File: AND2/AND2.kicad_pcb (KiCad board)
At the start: 2 copper layers, 31.7 x 27.9 mm, 13 parts, among them J1 In1, J2 In2, J3 Out, J4 Thru1, J5 Thru2, U1 And2_NC7SZ08

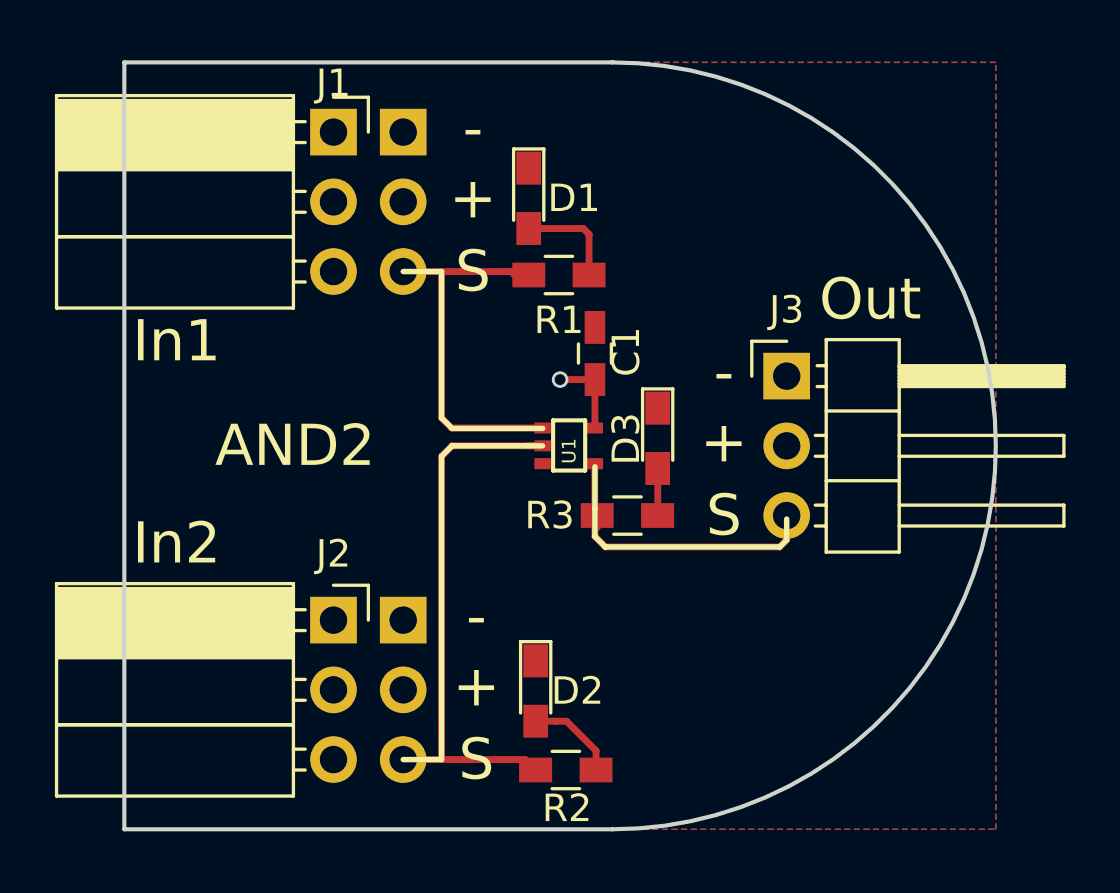
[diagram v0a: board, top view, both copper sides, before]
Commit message: Made XOR Board and modified FA
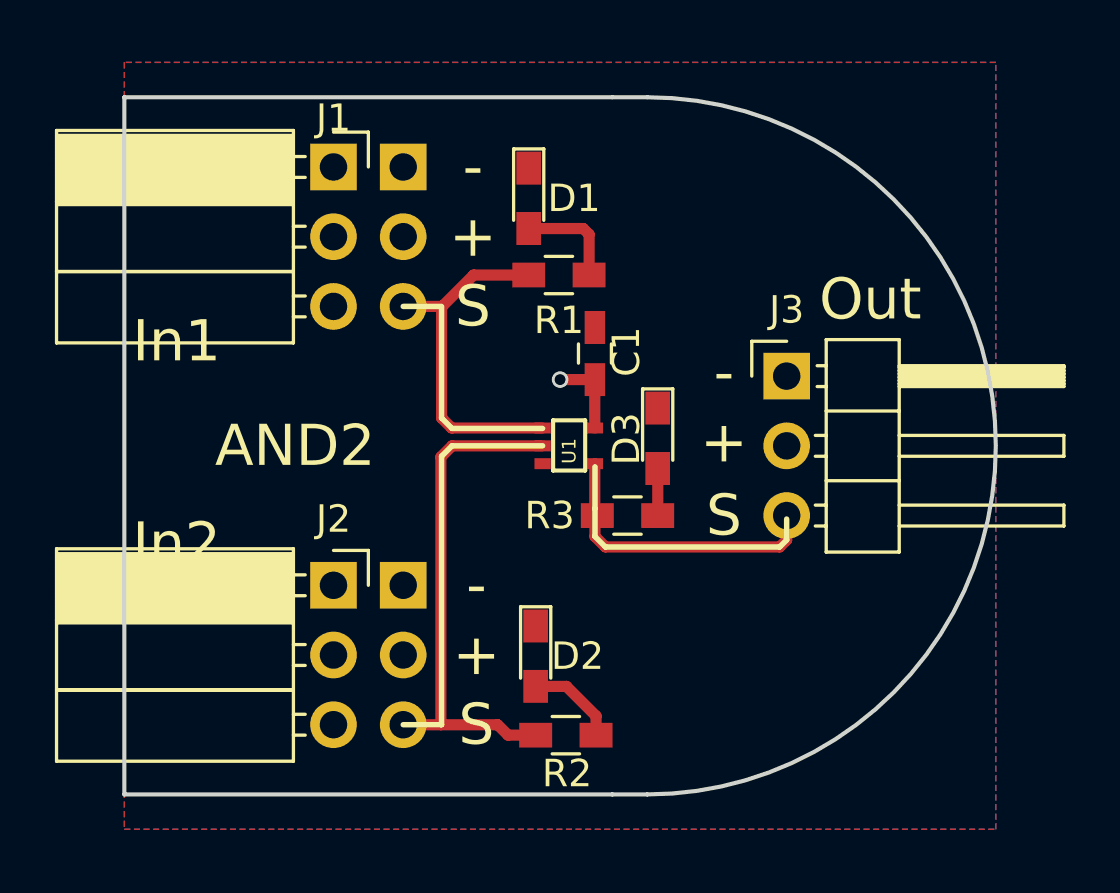
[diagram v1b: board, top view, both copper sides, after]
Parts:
- moved J2 1.27 mm to (129.5, 115.6)
- moved J5 1.27 mm to (132.1, 115.6)
- moved D2 1.27 mm to (136.9, 118.2)
- moved J1 1.27 mm to (129.5, 100.3)
- moved J4 1.27 mm to (132.1, 100.3)
- moved R2 1.27 mm to (138.0, 121.0)
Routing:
- net /In2: track 20.4 -> 19.2 mm
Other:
- board size 31.7 x 27.9 mm -> 31.7 x 25.4 mm
